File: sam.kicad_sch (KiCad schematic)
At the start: 39 parts, among them IC1 4164, IC15 MC6883, IC16 74LS244N, IC2 4164, IC3 4164, IC31 74LS02N, IC33 74LS138N, IC4 4164, IC5 4164, IC6 4164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

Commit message: repack layout
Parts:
- added JP5: Z8hi/low, Jumper:SolderJumper-3_P1.3mm_Bridged12_Pad1.0x1.5mm, symbol Jumper:Jumper_3_Bridged12
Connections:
- net +5V: now also JP5.1 (A); no longer IC1.1 (VBB), IC2.1 (VBB), IC3.1 (VBB), IC4.1 (VBB), IC5.1 (VBB), IC6.1 (VBB), IC7.1 (VBB), IC8.1 (VBB)
- net GND: now also JP5.3 (B)
- new net Z8: IC1.1 (VBB), IC2.1 (VBB), IC3.1 (VBB), IC4.1 (VBB), IC5.1 (VBB), IC6.1 (VBB), IC7.1 (VBB), IC8.1 (VBB), JP5.2 (C)

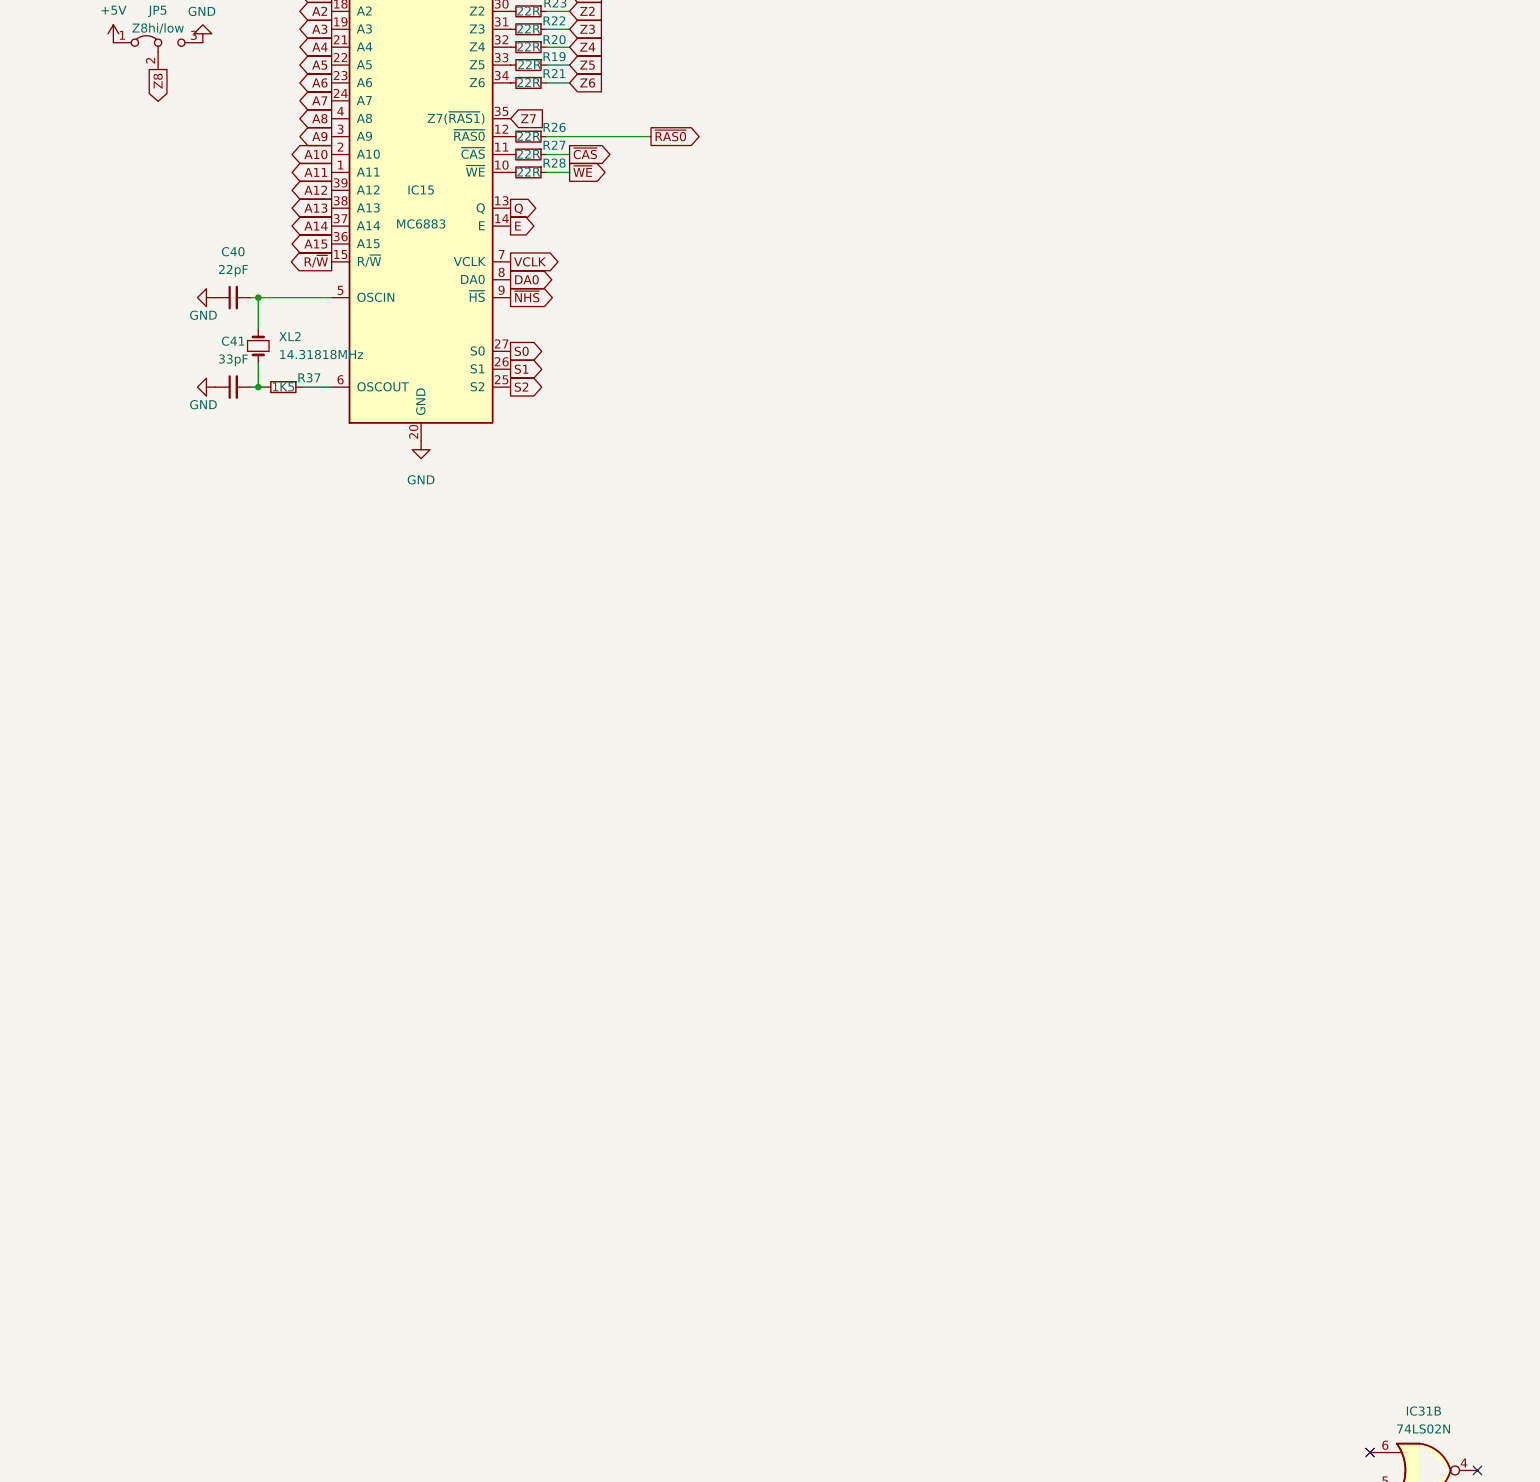
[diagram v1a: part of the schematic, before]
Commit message: add 256 banking
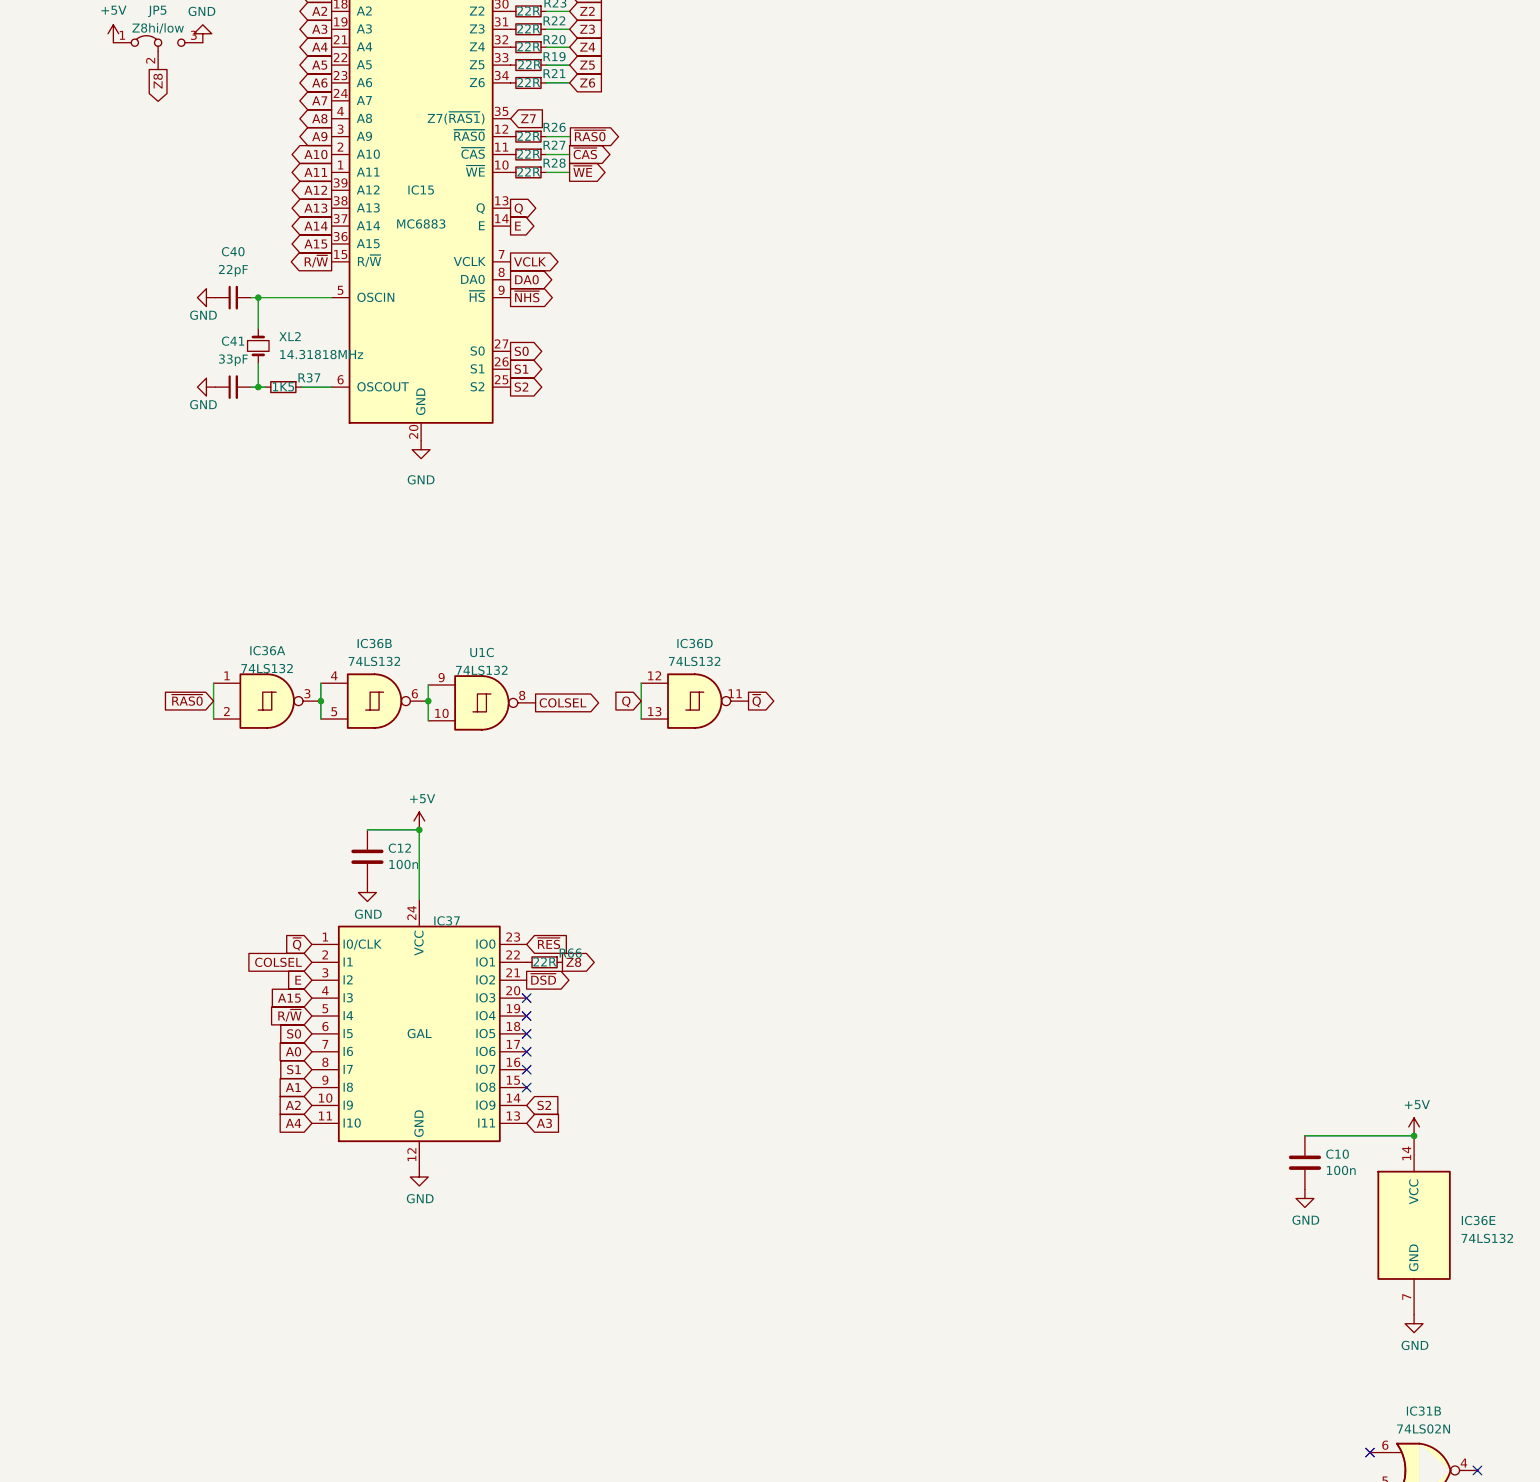
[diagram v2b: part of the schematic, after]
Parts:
- added C10, C12: 100n, Capacitor_THT:C_Rect_L7.0mm_W2.5mm_P5.00mm, symbol Device:C
- added IC36: 74LS132, Package_DIP:DIP-14_W7.62mm, symbol 74xx:74LS132
- added IC37: GAL, Package_DIP:DIP-24_W7.62mm, symbol vdg:GAL22V10
- added R66: 22R, Resistor_THT:R_Axial_DIN0207_L6.3mm_D2.5mm_P2.54mm_Vertical, symbol Device:R_Small
- added U1: 74LS132, symbol 74xx:74LS132
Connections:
- net +5V: now also C10.1, C12.1, IC36.14 (VCC), IC37.24 (VCC)
- net A0: now also IC37.7 (I6)
- net A1: now also IC37.9 (I8)
- net A15: now also IC37.4 (I3)
- net A2: now also IC37.10 (I9)
- net A3: now also IC37.13 (I11)
- net A4: now also IC37.11 (I10)
- net E: now also IC37.3 (I2)
- net GND: now also C10.2, C12.2, IC36.7 (GND), IC37.12 (GND)
- net Q: now also IC36.12, IC36.13
- net R/~{W}: now also IC37.5 (I4)
- net S0: now also IC37.6 (I5)
- net S1: now also IC37.8 (I7)
- net S2: now also IC37.14 (IO9)
- net Z8: now also R66.1
- net ~{RAS0}: now also IC36.1, IC36.2
- new net: IC36.3, IC36.4, IC36.5
- new net: IC36.6, U1.10, U1.9
- new net: IC37.22 (IO1), R66.2
- new net COLSEL: IC37.2 (I1), U1.8
- new net ~{DSD}: IC37.21 (IO2)
- new net ~{Q}: IC36.11, IC37.1 (I0/CLK)
- new net ~{RES}: IC37.23 (IO0)
- no-connect marks 4 -> 10

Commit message: handle 27C512
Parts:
- IC36: renamed from U1; footprint (none) -> Package_DIP:DIP-14_W7.62mm
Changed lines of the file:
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@@
     )
   )
-  (global_label "S2" (shape output) (at 88.773 163.576 180) (fields_autoplaced)
-    (effects (font (size 1.27 1.27)) (justify right))
-    (property "Intersheetrefs" "${INTERSHEET_REFS}" (at 84.0298 163.4966 0)
+  (global_label "S2" (shape input) (at 88.773 163.576 180) (fields_autoplaced)
+    (effects (font (size 1.27 1.27)) (justify right))
+    (property "Intersheetrefs" "${INTERSHEET_REFS}" (at 84.1024 163.576 0)
       (effects (font (size 1.27 1.27)) (justify right) hide)
     )
@@
     )
   )
-  (global_label "R{slash}~{W}" (shape output) (at 91.313 198.247 180) (fields_autoplaced)
-    (effects (font (size 1.27 1.27)) (justify right))
-    (property "Intersheetrefs" "${INTERSHEET_REFS}" (at 84.9369 198.1676 0)
+  (global_label "R{slash}~{W}" (shape input) (at 91.313 198.247 180) (fields_autoplaced)
+    (effects (font (size 1.27 1.27)) (justify right))
+    (property "Intersheetrefs" "${INTERSHEET_REFS}" (at 85.0095 198.247 0)
       (effects (font (size 1.27 1.27)) (justify right) hide)
     )
@@
     )
   )
-  (global_label "S0" (shape output) (at 109.347 158.496 180) (fields_autoplaced)
-    (effects (font (size 1.27 1.27)) (justify right))
-    (property "Intersheetrefs" "${INTERSHEET_REFS}" (at 104.6038 158.4166 0)
+  (global_label "S0" (shape input) (at 109.347 158.496 180) (fields_autoplaced)
+    (effects (font (size 1.27 1.27)) (justify right))
+    (property "Intersheetrefs" "${INTERSHEET_REFS}" (at 104.6764 158.496 0)
       (effects (font (size 1.27 1.27)) (justify right) hide)
     )
@@
     )
   )
-  (global_label "~{E17}" (shape input) (at 134.747 163.576 0) (fields_autoplaced)
-    (effects (font (size 1.27 1.27)) (justify left))
-    (property "Intersheetrefs" "${INTERSHEET_REFS}" (at 140.6393 163.4966 0)
+  (global_label "~{E17}" (shape output) (at 134.747 163.576 0) (fields_autoplaced)
+    (effects (font (size 1.27 1.27)) (justify left))
+    (property "Intersheetrefs" "${INTERSHEET_REFS}" (at 140.5666 163.576 0)
       (effects (font (size 1.27 1.27)) (justify left) hide)
     )
@@
     )
   )
-  (global_label "~{E18}" (shape input) (at 134.747 161.036 0) (fields_autoplaced)
-    (effects (font (size 1.27 1.27)) (justify left))
-    (property "Intersheetrefs" "${INTERSHEET_REFS}" (at 140.6393 160.9566 0)
+  (global_label "~{E18}" (shape output) (at 134.747 161.036 0) (fields_autoplaced)
+    (effects (font (size 1.27 1.27)) (justify left))
+    (property "Intersheetrefs" "${INTERSHEET_REFS}" (at 140.5666 161.036 0)
       (effects (font (size 1.27 1.27)) (justify left) hide)
     )
@@
     )
   )
-  (global_label "S1" (shape output) (at 109.347 161.036 180) (fields_autoplaced)
-    (effects (font (size 1.27 1.27)) (justify right))
-    (property "Intersheetrefs" "${INTERSHEET_REFS}" (at 104.6038 160.9566 0)
+  (global_label "S1" (shape input) (at 109.347 161.036 180) (fields_autoplaced)
+    (effects (font (size 1.27 1.27)) (justify right))
+    (property "Intersheetrefs" "${INTERSHEET_REFS}" (at 104.6764 161.036 0)
       (effects (font (size 1.27 1.27)) (justify right) hide)
     )
@@
     )
   )
-  (global_label "D.Out" (shape input) (at 134.747 158.496 0) (fields_autoplaced)
-    (effects (font (size 1.27 1.27)) (justify left))
-    (property "Intersheetrefs" "${INTERSHEET_REFS}" (at 142.1512 158.4166 0)
+  (global_label "D.Out" (shape output) (at 134.747 158.496 0) (fields_autoplaced)
+    (effects (font (size 1.27 1.27)) (justify left))
+    (property "Intersheetrefs" "${INTERSHEET_REFS}" (at 142.0786 158.496 0)
       (effects (font (size 1.27 1.27)) (justify left) hide)
     )
@@
   (symbol (lib_id "74xx:74LS132") (at 253.492 132.842 0) (unit 3)
     (in_bom yes) (on_board yes) (dnp no) (fields_autoplaced)
-    (property "Reference" "U1" (at 253.4837 125.73 0)
+    (property "Reference" "IC36" (at 253.4837 125.73 0)
       (effects (font (size 1.27 1.27)))
     )
@@
       (effects (font (size 1.27 1.27)))
     )
-    (property "Footprint" "" (at 253.492 132.842 0)
+    (property "Footprint" "Package_DIP:DIP-14_W7.62mm" (at 253.492 132.842 0)
       (effects (font (size 1.27 1.27)) hide)
     )
@@
       (project "Dragon32"
         (path "/0c3dceba-7c95-4b3d-b590-0eb581444beb/c0eaba02-6b8d-4a7f-b51d-5746c573781a"
-          (reference "U1") (unit 3)
-        )
-      )
+          (reference "IC36") (unit 3)
+        )
+      )
